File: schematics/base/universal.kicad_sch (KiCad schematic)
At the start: 14 parts, among them J1 Bionic_ZIF_Socket_48pin, SW1 Tact_SW, U1 TXS0108EPW, U2 TXS0108EPW, U3 TXS0108EPW, U4 TXS0108EPW, U5 TXS0108EPW

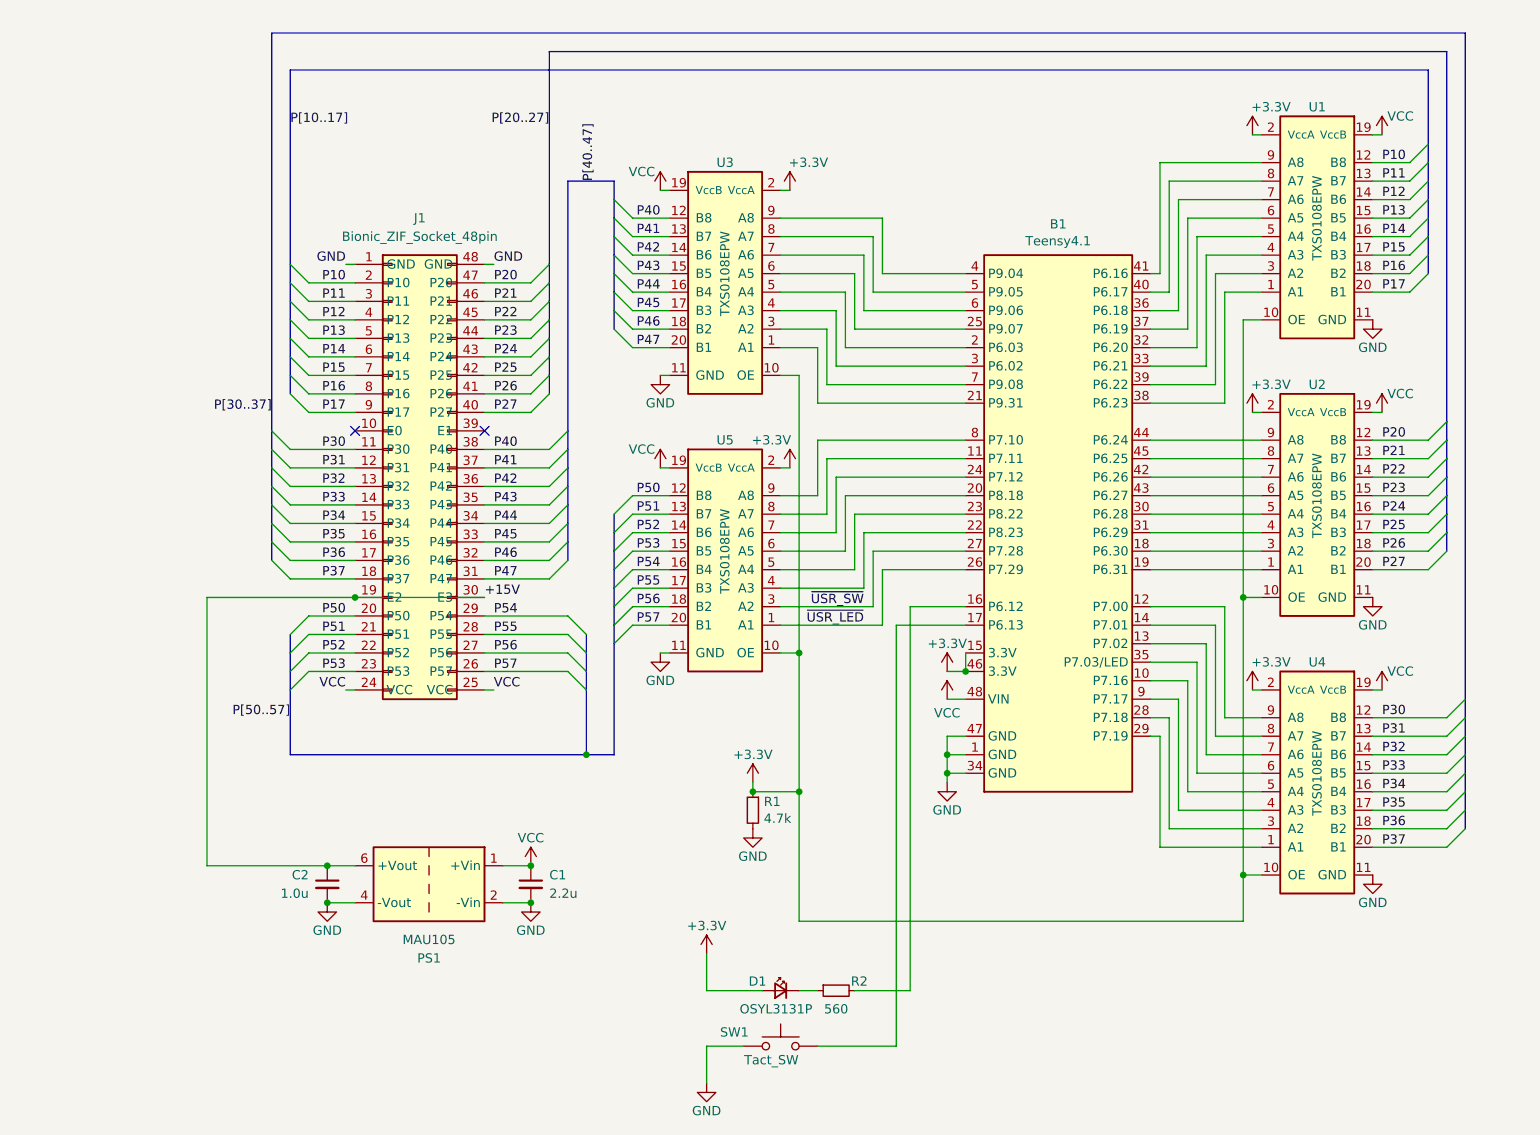
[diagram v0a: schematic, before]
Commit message: [Base] Add bus-terminaters
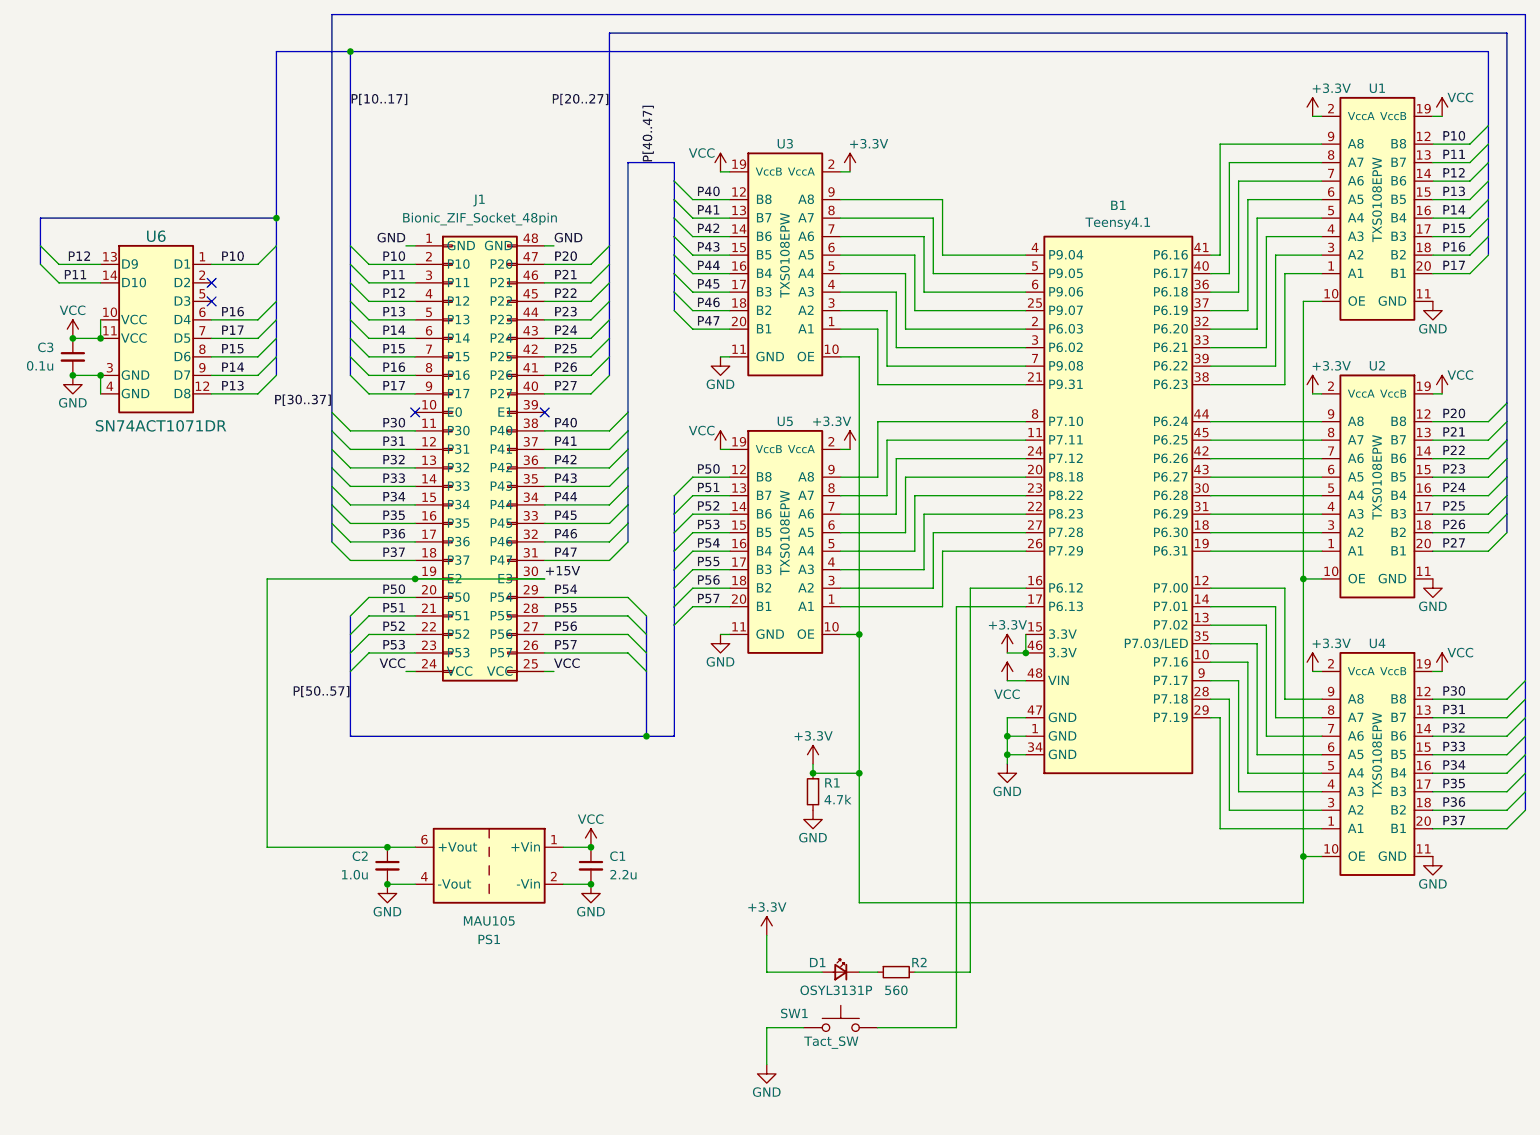
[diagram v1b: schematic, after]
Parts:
- added C3: 0.1u, Capacitor_THT:C_Disc_D3.4mm_W2.1mm_P2.50mm, symbol Device:C_Small
- added U6: SN74ACT1071DR, 0-LocalLibrary:DIP-14_W15.24mm_Socket, symbol ti:SN74ACT1071DR
- B1: footprint Package_DIP:DIP-48_W15.24mm -> 0-LocalLibrary:DIP-48_W15.24mm_Socket
- U1, U2, U3, U4, U5: footprint Package_SO:TSSOP-20_4.4x6.5mm_P0.65mm -> 0-LocalLibrary:DIP-20_W12.70mm_Socket
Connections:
- net GND: now also C3.2, U6.3 (GND), U6.4 (GND)
- net P10: now also U6.1 (D1)
- net P11: now also U6.14 (D10)
- net P12: now also U6.13 (D9)
- net P13: now also U6.12 (D8)
- net P14: now also U6.9 (D7)
- net P15: now also U6.8 (D6)
- net P16: now also U6.6 (D4)
- net P17: now also U6.7 (D5)
- net VCC: now also C3.1, U6.10 (VCC), U6.11 (VCC)
- net ~{USR_LED}: no longer names the net of B1.26 (P7.29), U5.1 (A1)
- net ~{USR_SW}: no longer names the net of B1.27 (P7.28), U5.3 (A2)
- no-connect marks 2 -> 4
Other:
- moved on the sheet: B1, C1, C2, D1, J1, PS1, R1, R2, SW1, U1, U2, U3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
